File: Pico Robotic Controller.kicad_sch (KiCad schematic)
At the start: 99 parts, among them J1 250-202, J10 Conn_02x03_Odd_Even, J11 250-202, J12 250-202, J13 Conn_02x05_Odd_Even, J2 conn_04_03, J3 250-203, J4 conn_04_03, J5 Conn_01x03, J6 Conn_01x02, J7 conn_04_03, J8 conn_04_03, J9 Conn_01x03, Q1 DMG2305UX-13, U1 Weewooday-820, U10 APX321WG-7, U11 74HC14, U12 74HC14, U13 PCA9685PW, U2 RPi_Pico_W, U3 RPi_Picobell_CAN_Bus, U4 PCA9685PW, U5 TCA9546, U6 Ethernet_FeatherWing, U7 TXS0104EPW, U8 TXS0104EPW, U9 APX321WG-7, X1 STEMMA_I2C_QT, X2 STEMMA_I2C_QT, X3 STEMMA_I2C_QT, X4 STEMMA_I2C_QT

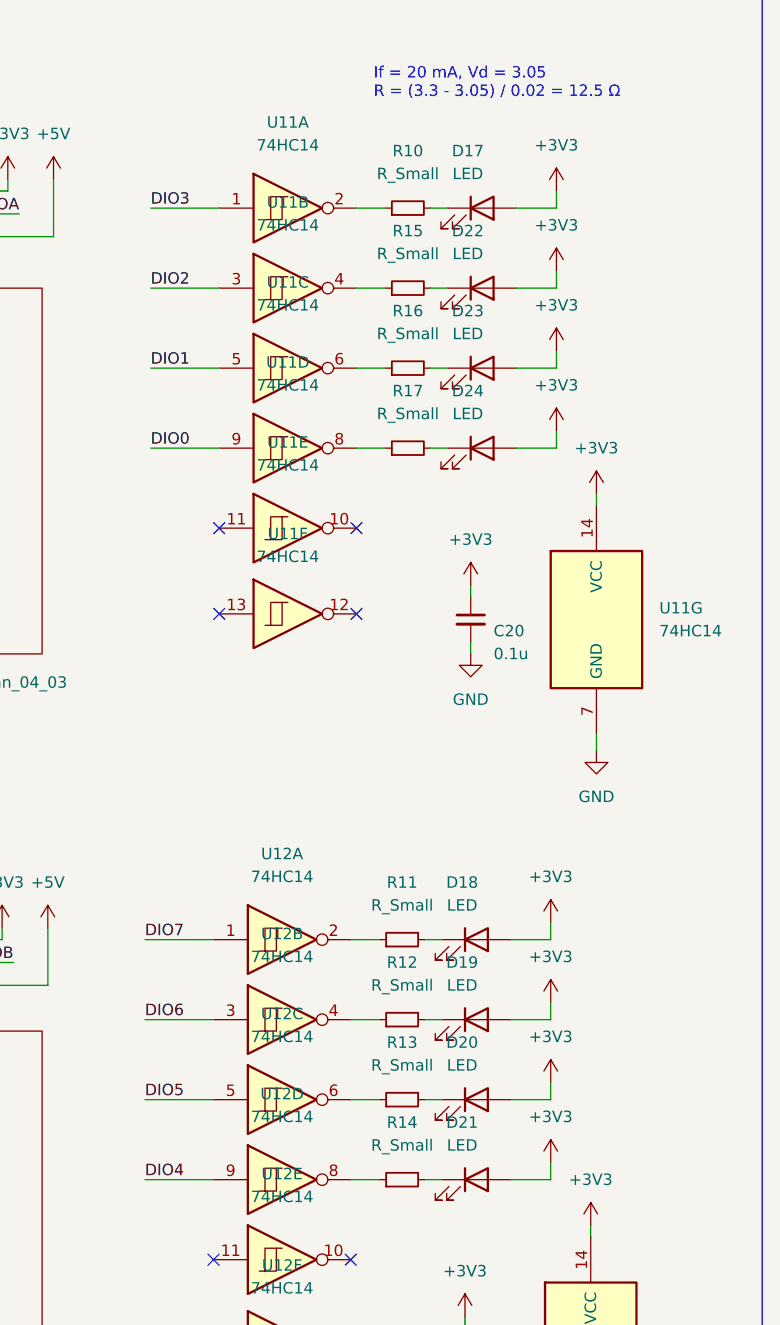
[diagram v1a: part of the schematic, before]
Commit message: updated LED resistor value (13 ohms)
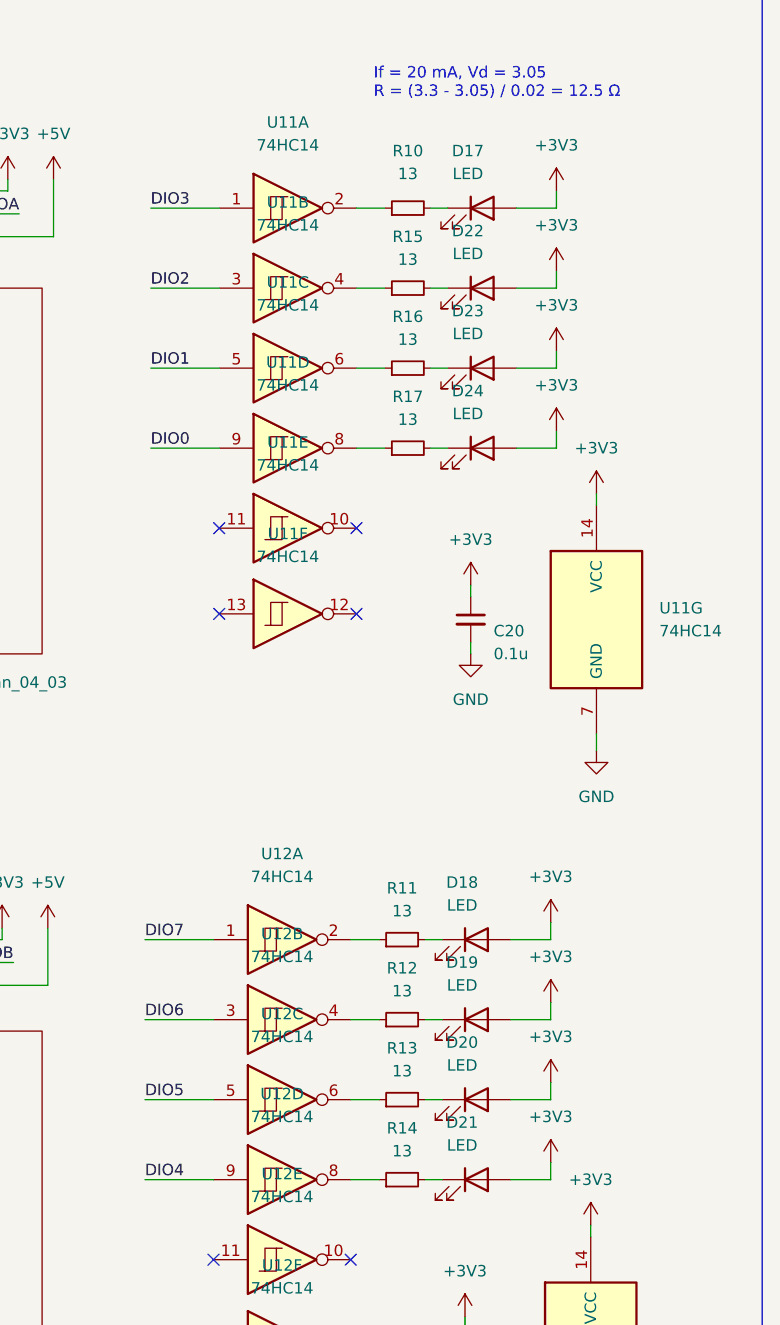
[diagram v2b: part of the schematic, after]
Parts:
- R10, R11, R12, R13, R14, R15, R16, R17: value R_Small -> 13
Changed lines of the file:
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@@
     (in_bom yes) (on_board yes) (fields_autoplaced)
     (property "Reference" "R10" (id 0) (at 541.02 34.925 90))
-    (property "Value" "R_Small" (id 1) (at 541.02 37.465 90))
+    (property "Value" "13" (id 1) (at 541.02 37.465 90))
     (property "Footprint" "Resistor_SMD:R_0603_1608Metric" (id 2) (at 541.02 41.275 0)
       (effects (font (size 1.27 1.27)) hide)
@@
   (symbol (lib_id "Device:R_Small") (at 540.385 149.225 90) (unit 1)
     (in_bom yes) (on_board yes) (fields_autoplaced)
-    (property "Reference" "R14" (id 0) (at 540.385 142.875 90))
-    (property "Value" "R_Small" (id 1) (at 540.385 145.415 90))
+    (property "Reference" "R14" (id 0) (at 540.385 143.51 90))
+    (property "Value" "13" (id 1) (at 540.385 146.05 90))
     (property "Footprint" "Resistor_SMD:R_0603_1608Metric" (id 2) (at 540.385 149.225 0)
       (effects (font (size 1.27 1.27)) hide)
@@
   (symbol (lib_id "Device:R_Small") (at 540.385 140.335 90) (unit 1)
     (in_bom yes) (on_board yes) (fields_autoplaced)
-    (property "Reference" "R13" (id 0) (at 540.385 133.985 90))
-    (property "Value" "R_Small" (id 1) (at 540.385 136.525 90))
+    (property "Reference" "R13" (id 0) (at 540.385 134.62 90))
+    (property "Value" "13" (id 1) (at 540.385 137.16 90))
     (property "Footprint" "Resistor_SMD:R_0603_1608Metric" (id 2) (at 540.385 140.335 0)
       (effects (font (size 1.27 1.27)) hide)
@@
   (symbol (lib_id "Device:R_Small") (at 541.02 67.945 90) (unit 1)
     (in_bom yes) (on_board yes) (fields_autoplaced)
-    (property "Reference" "R17" (id 0) (at 541.02 61.595 90))
-    (property "Value" "R_Small" (id 1) (at 541.02 64.135 90))
+    (property "Reference" "R17" (id 0) (at 541.02 62.23 90))
+    (property "Value" "13" (id 1) (at 541.02 64.77 90))
     (property "Footprint" "Resistor_SMD:R_0603_1608Metric" (id 2) (at 541.02 67.945 0)
       (effects (font (size 1.27 1.27)) hide)
@@
   (symbol (lib_id "Device:R_Small") (at 541.02 59.055 90) (unit 1)
     (in_bom yes) (on_board yes) (fields_autoplaced)
-    (property "Reference" "R16" (id 0) (at 541.02 52.705 90))
-    (property "Value" "R_Small" (id 1) (at 541.02 55.245 90))
+    (property "Reference" "R16" (id 0) (at 541.02 53.34 90))
+    (property "Value" "13" (id 1) (at 541.02 55.88 90))
     (property "Footprint" "Resistor_SMD:R_0603_1608Metric" (id 2) (at 541.02 59.055 0)
       (effects (font (size 1.27 1.27)) hide)
@@
   (symbol (lib_id "Device:R_Small") (at 540.385 122.555 90) (unit 1)
     (in_bom yes) (on_board yes) (fields_autoplaced)
-    (property "Reference" "R11" (id 0) (at 540.385 116.205 90))
-    (property "Value" "R_Small" (id 1) (at 540.385 118.745 90))
+    (property "Reference" "R11" (id 0) (at 540.385 116.84 90))
+    (property "Value" "13" (id 1) (at 540.385 119.38 90))
     (property "Footprint" "Resistor_SMD:R_0603_1608Metric" (id 2) (at 540.385 122.555 0)
       (effects (font (size 1.27 1.27)) hide)
@@
   (symbol (lib_id "Device:R_Small") (at 541.02 50.165 90) (unit 1)
     (in_bom yes) (on_board yes) (fields_autoplaced)
-    (property "Reference" "R15" (id 0) (at 541.02 43.815 90))
-    (property "Value" "R_Small" (id 1) (at 541.02 46.355 90))
+    (property "Reference" "R15" (id 0) (at 541.02 44.45 90))
+    (property "Value" "13" (id 1) (at 541.02 46.99 90))
     (property "Footprint" "Resistor_SMD:R_0603_1608Metric" (id 2) (at 541.02 50.165 0)
       (effects (font (size 1.27 1.27)) hide)
@@
   (symbol (lib_id "Device:R_Small") (at 540.385 131.445 90) (unit 1)
     (in_bom yes) (on_board yes) (fields_autoplaced)
-    (property "Reference" "R12" (id 0) (at 540.385 125.095 90))
-    (property "Value" "R_Small" (id 1) (at 540.385 127.635 90))
+    (property "Reference" "R12" (id 0) (at 540.385 125.73 90))
+    (property "Value" "13" (id 1) (at 540.385 128.27 90))
     (property "Footprint" "Resistor_SMD:R_0603_1608Metric" (id 2) (at 540.385 131.445 0)
       (effects (font (size 1.27 1.27)) hide)
@@
     )
     (path "/050a4802-6ddc-4140-ad41-dadd85d26795"
-      (reference "R10") (unit 1) (value "R_Small") (footprint "Resistor_SMD:R_0603_1608Metric")
+      (reference "R10") (unit 1) (value "13") (footprint "Resistor_SMD:R_0603_1608Metric")
     )
     (path "/d6574822-48ea-4c7e-ac36-2471888a0397"
-      (reference "R11") (unit 1) (value "R_Small") (footprint "Resistor_SMD:R_0603_1608Metric")
+      (reference "R11") (unit 1) (value "13") (footprint "Resistor_SMD:R_0603_1608Metric")
     )
     (path "/e8742fa7-f4ac-45e1-ade1-d30e73fe4eeb"
-      (reference "R12") (unit 1) (value "R_Small") (footprint "Resistor_SMD:R_0603_1608Metric")
+      (reference "R12") (unit 1) (value "13") (footprint "Resistor_SMD:R_0603_1608Metric")
     )
     (path "/289578b1-259e-45e7-9b35-fd3dbd9b8b7c"
-      (reference "R13") (unit 1) (value "R_Small") (footprint "Resistor_SMD:R_0603_1608Metric")
+      (reference "R13") (unit 1) (value "13") (footprint "Resistor_SMD:R_0603_1608Metric")
     )
     (path "/0a9db80c-f0d2-4bd6-b581-868ba90600dc"
-      (reference "R14") (unit 1) (value "R_Small") (footprint "Resistor_SMD:R_0603_1608Metric")
+      (reference "R14") (unit 1) (value "13") (footprint "Resistor_SMD:R_0603_1608Metric")
     )
     (path "/e667fd23-ae57-423e-80ac-71d2d3ad2463"
-      (reference "R15") (unit 1) (value "R_Small") (footprint "Resistor_SMD:R_0603_1608Metric")
+      (reference "R15") (unit 1) (value "13") (footprint "Resistor_SMD:R_0603_1608Metric")
     )
     (path "/937f1bad-be1c-4d02-96af-716075228d7e"
-      (reference "R16") (unit 1) (value "R_Small") (footprint "Resistor_SMD:R_0603_1608Metric")
+      (reference "R16") (unit 1) (value "13") (footprint "Resistor_SMD:R_0603_1608Metric")
     )
     (path "/89d973d3-94cd-4e2c-9c83-d683ed79dad2"
-      (reference "R17") (unit 1) (value "R_Small") (footprint "Resistor_SMD:R_0603_1608Metric")
+      (reference "R17") (unit 1) (value "13") (footprint "Resistor_SMD:R_0603_1608Metric")
     )
     (path "/fbf78470-504e-46dd-93fd-6002533154c8"

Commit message: updated KiCAD design files to add separate OEn for motor PWM generator
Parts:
- added R18: 5K1, Resistor_SMD:R_1206_3216Metric, symbol Device:R_Small
- D10, D11, D12, D13, D14, D15, D2, D4, D5, D6, D7, D8, D9: Reference_1 (none) -> D; Value_1 (none) -> PESD1CAN-UX
- U5: footprint Package_SO:TSSOP-16_4.4x5mm_P0.65mm -> Package_SO:SOIC-16_3.9x9.9mm_P1.27mm
- U7, U8: footprint Package_SO:TSSOP-14_4.4x5mm_P0.65mm -> Package_SO:TSSOP-14-1EP_4.4x5mm_P0.65mm
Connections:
- net GND: now also R18.1
- net PWM_OEn: now also R18.2; no longer R3.2, U13.23 (~{OE})
- net MOTOR_OEn: now reaches U2.34 (GP28/ADC2)
- net MOTOR_OEn: now also R3.2, U13.23 (~{OE})
- no-connect marks 79 -> 78

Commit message: updated the PWM generator enables to be pull ups from pull down
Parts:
- D10, D11, D12, D13, D14, D15, D2, D4, D5, D6, D7, D8, D9: Reference_1 D -> (none)
- J1, J11, J12: footprint 250202 -> Appreciate:250202
- J3: footprint 250-203_1 -> Appreciate:250-203_1
- U5: footprint Package_SO:SOIC-16_3.9x9.9mm_P1.27mm -> Package_SO:TSSOP-16_4.4x5mm_P0.65mm
- U7, U8: footprint Package_SO:TSSOP-14-1EP_4.4x5mm_P0.65mm -> Package_SO:TSSOP-14_4.4x5mm_P0.65mm
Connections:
- net +3V3: now also R18.1, R3.1
- net GND: no longer R18.1, R3.1
